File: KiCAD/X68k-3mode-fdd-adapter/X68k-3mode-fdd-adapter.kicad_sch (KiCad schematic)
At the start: 99 parts, among them J101 4pin, J102 Conn_02x06_Odd_Even, J103 Conn_01x02, J104 Conn_01x04, J105 Conn_01x02, J106 Conn_02x17_Odd_Even, J107 Conn_02x17_Odd_Even, J108 Conn_02x17_Odd_Even, J109 Conn_01x03, Q102 2SC2712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

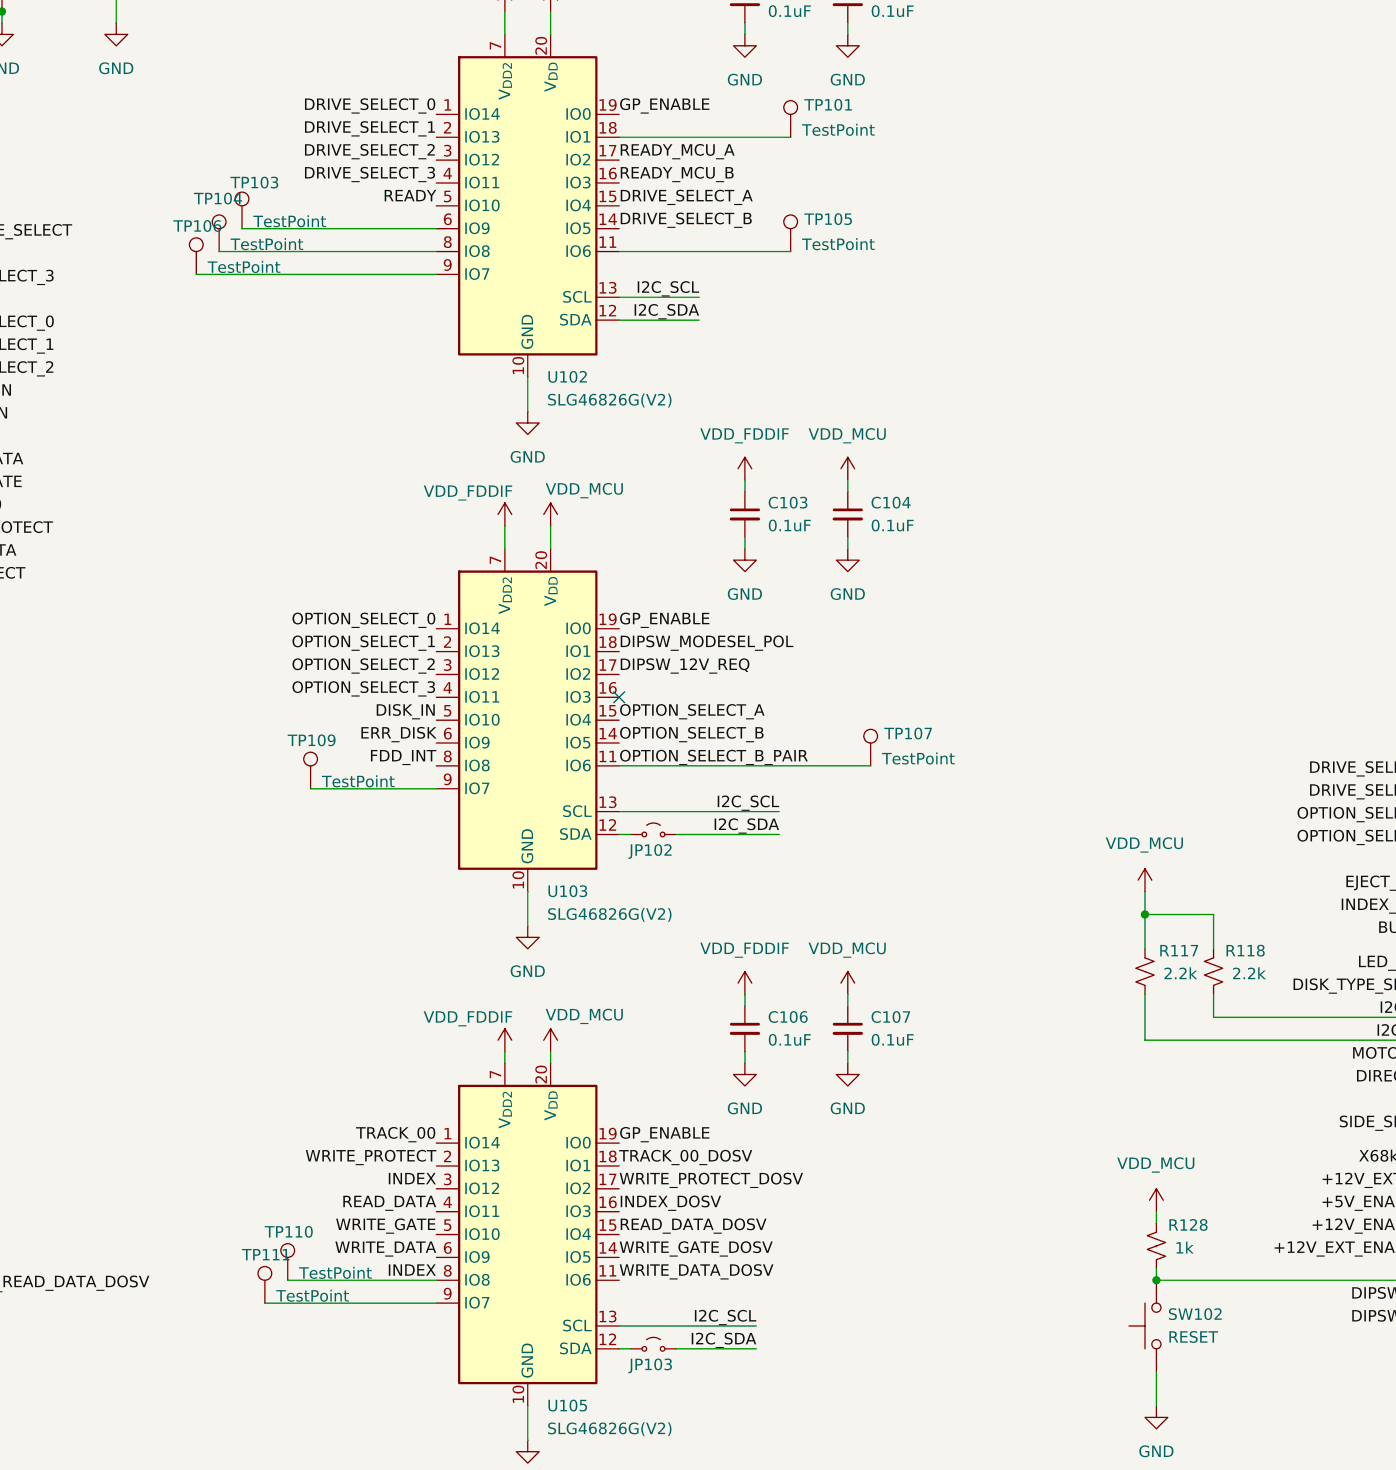
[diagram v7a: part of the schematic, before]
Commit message: メディアの論理イジェクトができるようにコードと回路を少し修正した(未確認)
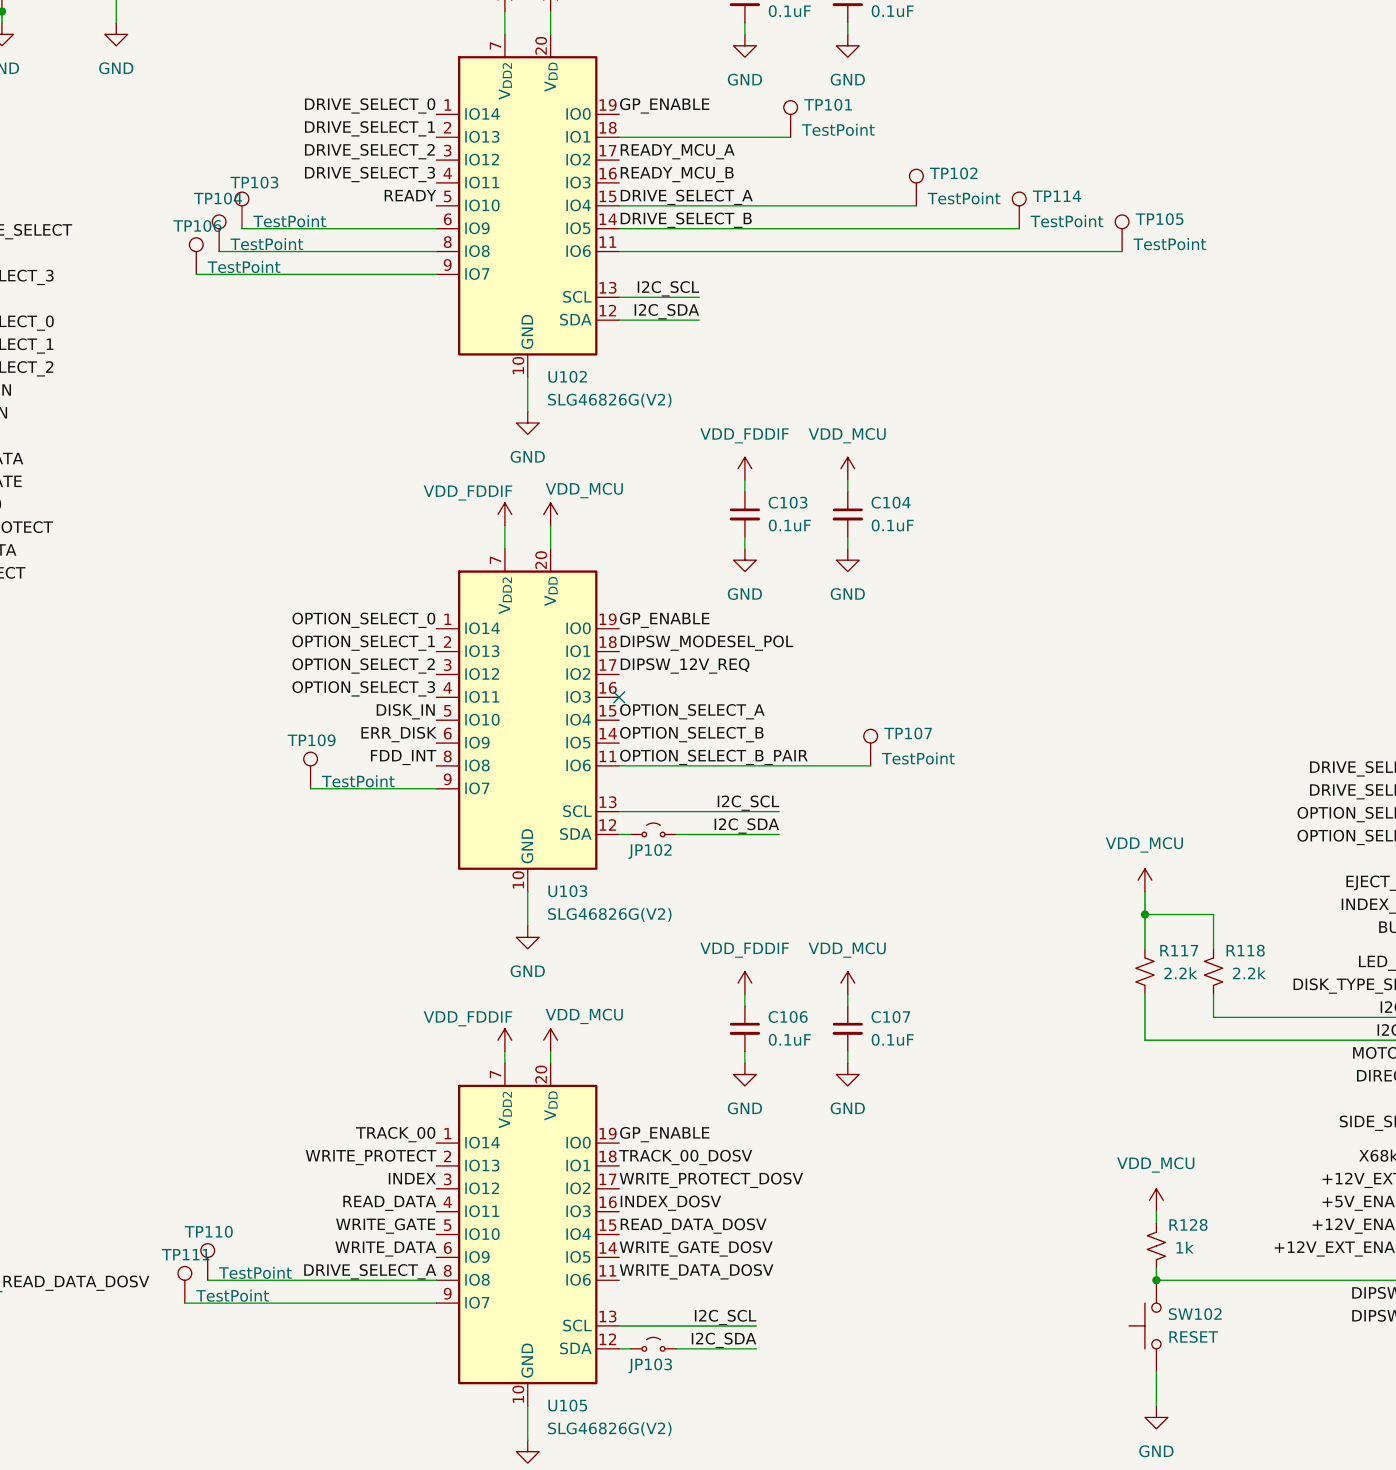
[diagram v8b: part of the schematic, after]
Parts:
- added TP102, TP114: TestPoint, TestPoint:TestPoint_Pad_1.0x1.0mm, symbol Connector:TestPoint
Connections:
- net DRIVE_SELECT_A: now also TP110.1, U105.8 (IO8), TP102.1
- net DRIVE_SELECT_B: now also TP114.1
- net INDEX: no longer TP110.1, U105.8 (IO8)
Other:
- moved on the sheet: TP105, TP110, TP111
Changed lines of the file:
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@@
 	(wire
 		(pts
-			(xy 97.79 252.73) (xy 114.3 252.73)
+			(xy 88.9 252.73) (xy 114.3 252.73)
 		)
 		(stroke
@@
 	(wire
 		(pts
+			(xy 134.62 133.35) (xy 167.64 133.35)
+		)
+		(stroke
+			(width 0)
+			(type default)
+		)
+	)
+	(wire
+		(pts
 			(xy 256.54 246.38) (xy 287.02 246.38)
 		)
@@
 	(wire
 		(pts
-			(xy 134.62 138.43) (xy 153.67 138.43)
+			(xy 134.62 138.43) (xy 190.5 138.43)
 		)
 		(stroke
@@
 	(wire
 		(pts
-			(xy 95.25 255.27) (xy 114.3 255.27)
+			(xy 86.36 255.27) (xy 114.3 255.27)
 		)
 		(stroke
@@
 	(wire
 		(pts
+			(xy 134.62 135.89) (xy 179.07 135.89)
+		)
+		(stroke
+			(width 0)
+			(type default)
+		)
+	)
+	(wire
+		(pts
 			(xy 52.07 213.36) (xy 52.07 215.9)
 		)
@@
 		)
 	)
+	(label "DRIVE_SELECT_A"
+		(at 114.3 252.73 180)
+		(effects
+			(font
+				(size 1.27 1.27)
+			)
+			(justify right bottom)
+		)
+	)
 	(label "EJECT"
 		(at 35.56 238.76 180)
@@
 		)
 	)
-	(label "INDEX"
-		(at 114.3 252.73 180)
-		(effects
-			(font
-				(size 1.27 1.27)
-			)
-			(justify right bottom)
-		)
-	)
 	(label "WRITE_DATA"
 		(at 35.56 248.92 180)
@@
 	)
 	(symbol
+		(lib_id "Connector:TestPoint")
+		(at 179.07 135.89 0)
+		(unit 1)
+		(exclude_from_sim no)
+		(in_bom yes)
+		(on_board yes)
+		(dnp no)
+		(property "Reference" "TP114"
+			(at 180.594 132.334 0)
+			(effects
+				(font
+					(size 1.27 1.27)
+				)
+				(justify left)
+			)
+		)
+		(property "Value" "TestPoint"
+			(at 180.34 135.128 0)
+			(effects
+				(font
+					(size 1.27 1.27)
+				)
+				(justify left)
+			)
+		)
+		(property "Footprint" "TestPoint:TestPoint_Pad_1.0x1.0mm"
+			(at 184.15 135.89 0)
+			(effects
+				(font
+					(size 1.27 1.27)
+				)
+				(hide yes)
+			)
+		)
+		(property "Datasheet" "~"
+			(at 184.15 135.89 0)
+			(effects
+				(font
+					(size 1.27 1.27)
+				)
+				(hide yes)
+			)
+		)
+		(property "Description" "test point"
+			(at 179.07 135.89 0)
+			(effects
+				(font
+					(size 1.27 1.27)
+				)
+				(hide yes)
+			)
+		)
+		(property "LCIC" ""
+			(at 179.07 135.89 0)
+			(effects
+				(font
+					(size 1.27 1.27)
+				)
+				(hide yes)
+			)
+		)
+		(pin "1"
+		)
+		(instances
+			(project "X68k-3mode-fdd-adapter"
+				(path "/13b3a4ee-84d6-44b3-962d-9cf7c36d7564"
+					(reference "TP114")
+					(unit 1)
+				)
+			)
+		)
+	)
+	(symbol
 		(lib_id "power:GND")
 		(at 392.43 92.71 270)
@@
 	(symbol
 		(lib_id "Connector:TestPoint")
-		(at 97.79 252.73 0)
+		(at 88.9 252.73 0)
 		(unit 1)
 		(exclude_from_sim no)
@@
 		(dnp no)
 		(property "Reference" "TP110"
-			(at 95.25 247.396 0)
+			(at 86.36 247.396 0)
 			(effects
 				(font
@@
 		)
 		(property "Value" "TestPoint"
-			(at 99.06 251.968 0)
+			(at 90.17 251.968 0)
 			(effects
 				(font
@@
 		)
 		(property "Footprint" "TestPoint:TestPoint_Pad_1.0x1.0mm"
-			(at 102.87 252.73 0)
+			(at 93.98 252.73 0)
 			(effects
 				(font
@@
 		)
 		(property "Datasheet" "~"
-			(at 102.87 252.73 0)
+			(at 93.98 252.73 0)
 			(effects
 				(font
@@
 		)
 		(property "Description" "test point"
-			(at 97.79 252.73 0)
+			(at 88.9 252.73 0)
 			(effects
 				(font
@@
 		)
 		(property "LCIC" ""
-			(at 97.79 252.73 0)
+			(at 88.9 252.73 0)
 			(effects
 				(font
@@
 	)
 	(symbol
+		(lib_id "Connector:TestPoint")
+		(at 167.64 133.35 0)
+		(unit 1)
+		(exclude_from_sim no)
+		(in_bom yes)
+		(on_board yes)
+		(dnp no)
+		(property "Reference" "TP102"
+			(at 169.164 129.794 0)
+			(effects
+				(font
+					(size 1.27 1.27)
+				)
+				(justify left)
+			)
+		)
+		(property "Value" "TestPoint"
+			(at 168.91 132.588 0)
+			(effects
+				(font
+					(size 1.27 1.27)
+				)
+				(justify left)
+			)
+		)
+		(property "Footprint" "TestPoint:TestPoint_Pad_1.0x1.0mm"
+			(at 172.72 133.35 0)
+			(effects
+				(font
+					(size 1.27 1.27)
+				)
+				(hide yes)
+			)
+		)
+		(property "Datasheet" "~"
+			(at 172.72 133.35 0)
+			(effects
+				(font
+					(size 1.27 1.27)
+				)
+				(hide yes)
+			)
+		)
+		(property "Description" "test point"
+			(at 167.64 133.35 0)
+			(effects
+				(font
+					(size 1.27 1.27)
+				)
+				(hide yes)
+			)
+		)
+		(property "LCIC" ""
+			(at 167.64 133.35 0)
+			(effects
+				(font
+					(size 1.27 1.27)
+				)
+				(hide yes)
+			)
+		)
+		(pin "1"
+		)
+		(instances
+			(project "X68k-3mode-fdd-adapter"
+				(path "/13b3a4ee-84d6-44b3-962d-9cf7c36d7564"
+					(reference "TP102")
+					(unit 1)
+				)
+			)
+		)
+	)
+	(symbol
 		(lib_id "power:GND")
 		(at 295.91 46.99 0)
@@
 	(symbol
 		(lib_id "Connector:TestPoint")
-		(at 153.67 138.43 0)
+		(at 190.5 138.43 0)
 		(unit 1)
 		(exclude_from_sim no)
@@
 		(dnp no)
 		(property "Reference" "TP105"
-			(at 155.194 134.874 0)
+			(at 192.024 134.874 0)
 			(effects
 				(font
@@
 		)
 		(property "Value" "TestPoint"
-			(at 154.94 137.668 0)
+			(at 191.77 137.668 0)
 			(effects
 				(font
@@
 		)
 		(property "Footprint" "TestPoint:TestPoint_Pad_1.0x1.0mm"
-			(at 158.75 138.43 0)
+			(at 195.58 138.43 0)
 			(effects
 				(font
@@
 		)
 		(property "Datasheet" "~"
-			(at 158.75 138.43 0)
+			(at 195.58 138.43 0)
 			(effects
 				(font
@@
 		)
 		(property "Description" "test point"
-			(at 153.67 138.43 0)
+			(at 190.5 138.43 0)
 			(effects
 				(font
@@
 		)
 		(property "LCIC" ""
-			(at 153.67 138.43 0)
+			(at 190.5 138.43 0)
 			(effects
 				(font
@@
 	(symbol
 		(lib_id "Connector:TestPoint")
-		(at 95.25 255.27 0)
+		(at 86.36 255.27 0)
 		(unit 1)
 		(exclude_from_sim no)
@@
 		(dnp no)
 		(property "Reference" "TP111"
-			(at 92.71 249.936 0)
+			(at 83.82 249.936 0)
 			(effects
 				(font
@@
 		)
 		(property "Value" "TestPoint"
-			(at 96.52 254.508 0)
+			(at 87.63 254.508 0)
 			(effects
 				(font
@@
 		)
 		(property "Footprint" "TestPoint:TestPoint_Pad_1.0x1.0mm"
-			(at 100.33 255.27 0)
+			(at 91.44 255.27 0)
 			(effects
 				(font
@@
 		)
 		(property "Datasheet" "~"
-			(at 100.33 255.27 0)
+			(at 91.44 255.27 0)
 			(effects
 				(font
@@
 		)
 		(property "Description" "test point"
-			(at 95.25 255.27 0)
+			(at 86.36 255.27 0)
 			(effects
 				(font
@@
 		)
 		(property "LCIC" ""
-			(at 95.25 255.27 0)
+			(at 86.36 255.27 0)
 			(effects
 				(font
